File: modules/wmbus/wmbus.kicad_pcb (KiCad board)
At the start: 2 copper layers, 27.9 x 28.6 mm, 15 parts, among them J1 Conn_01x08, J2 Conn_01x08, U2 RC-S2LP-868

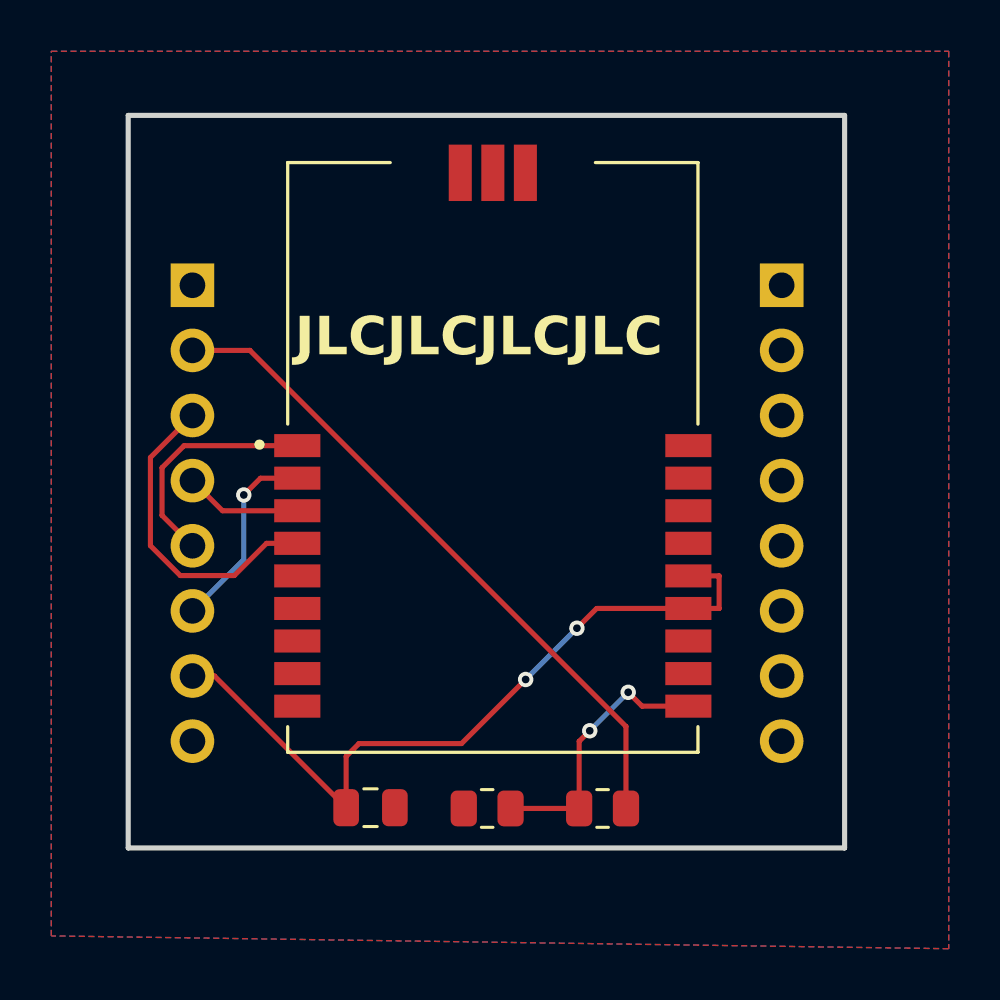
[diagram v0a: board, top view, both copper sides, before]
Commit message: feat: add wmbus module
Signed-off-by: Rodney Osodo <socials@rodneyosodo.com>
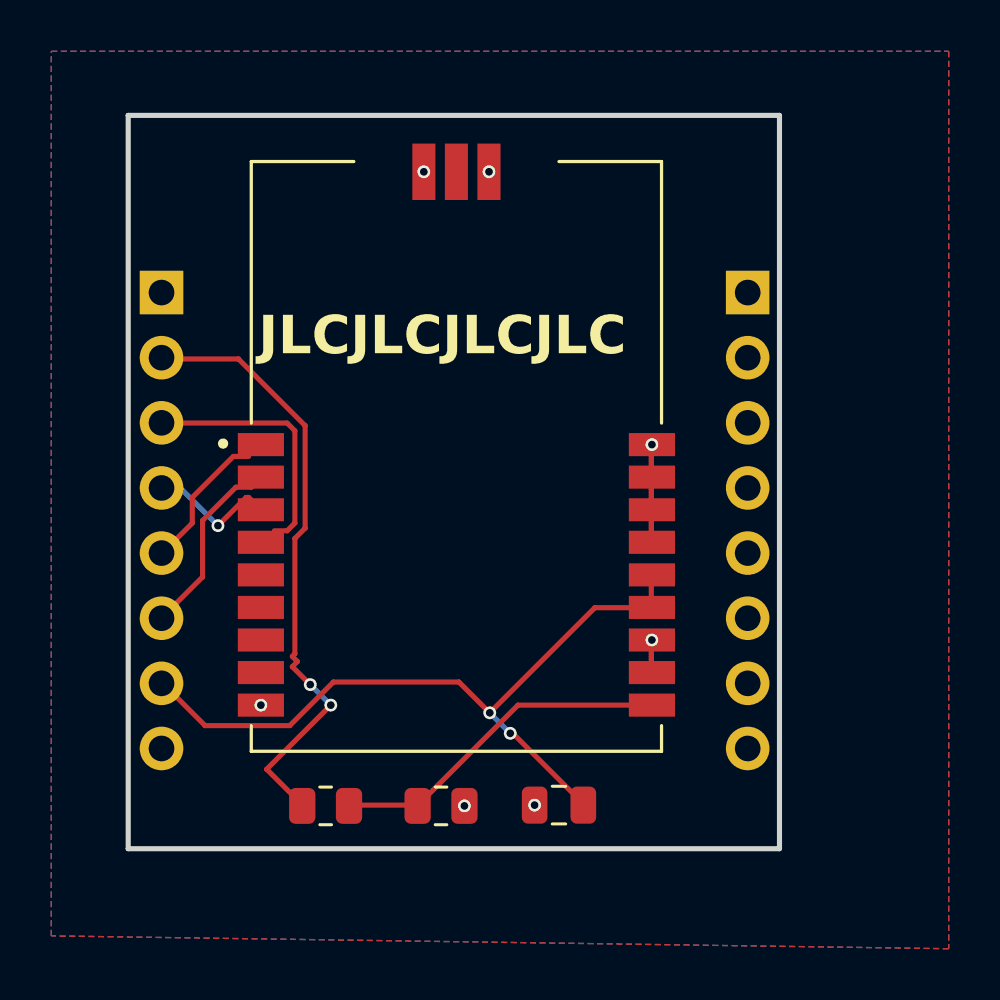
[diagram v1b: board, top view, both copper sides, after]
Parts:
- moved R1 10.8 mm to (55.7, 129.4), turned to 0 degrees
- moved C1 7.35 mm to (64.8, 129.4), turned to 180 degrees
- moved R2 1.80 mm to (60.2, 129.4), turned to 0 degrees
- moved kibuzzard-6A563BEF 1.51 mm to (60.7, 105.6)
- moved U2 1.42 mm to (60.8, 115.8)
- moved J2 1.36 mm to (72.2, 109.4)
- moved kibuzzard-6A563B50 1.26 mm to (53.4, 117.0)
- moved kibuzzard-6A563B65 1.26 mm to (54.0, 119.6)
- moved kibuzzard-6A563B31 1.26 mm to (53.3, 111.9)
- moved kibuzzard-6A563B41 1.26 mm to (52.7, 114.5)
- moved kibuzzard-6A563B71 1.26 mm to (53.9, 122.2)
- moved kibuzzard-6A563B7D 1.26 mm to (53.8, 124.7)
- moved kibuzzard-6A563B88 1.26 mm to (53.2, 127.3)
- moved J1 1.24 mm to (49.3, 109.4)
- moved kibuzzard-6A563B96 1.10 mm to (68.3, 127.3)
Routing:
- net GND: track 0.00 -> 5.41 mm, vias 0 -> 7
- net MISO: track 9.17 -> 5.61 mm
- net Net-(U2-SDN): track 10.6 -> 13.5 mm, vias 2 -> 0
- net CS: track 12.5 -> 9.90 mm
- net SDN: track 26.2 -> 24.1 mm, vias 0 -> 2
- net SCK: track 4.58 -> 5.22 mm, vias 0 -> 1
- net MOSI: track 7.71 -> 7.49 mm, vias 1 -> 0
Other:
- board size 27.9 x 28.6 mm -> 25.4 x 28.6 mm

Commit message: cross check wmbus module is ready for fabrication
Signed-off-by: Rodney Osodo <socials@rodneyosodo.com>
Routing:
- net SCK: track 5.22 -> 10.4 mm, vias 1 -> 0
- net GND: track 5.41 -> 9.64 mm, vias 7 -> 10
- net CS: track 9.90 -> 11.0 mm
- net SDN: track 24.1 -> 24.6 mm
